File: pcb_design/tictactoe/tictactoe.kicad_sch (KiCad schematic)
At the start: 9 parts

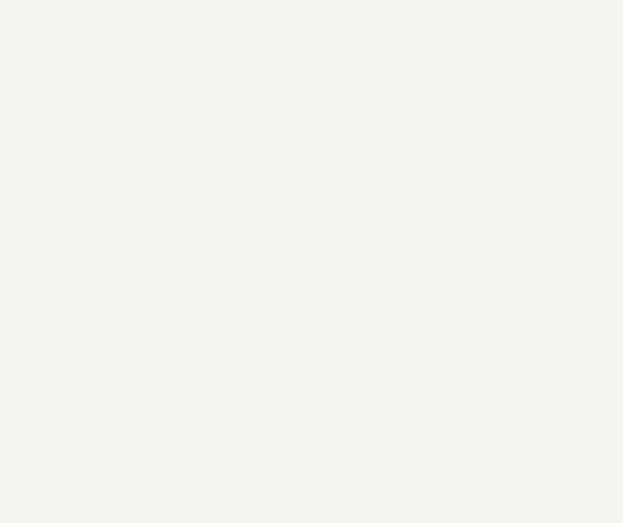
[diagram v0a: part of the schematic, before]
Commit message: NH: Added tactile button to schematic
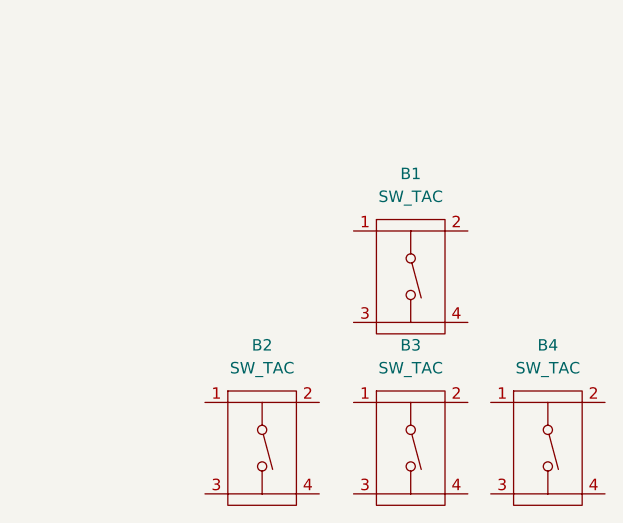
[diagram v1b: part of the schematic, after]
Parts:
- added B1, B2, B3, B4: SW_TAC, symbol TicTacToe:SW_TAC
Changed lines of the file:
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@@
+    (pin "4")
+  )
+  (symbol (lib_id "TicTacToe:SW_TAC") (at 214.63 133.35 0) (unit 1)
+    (in_bom yes) (on_board yes) (fields_autoplaced)
+    (property "Reference" "B2" (id 0) (at 214.63 129.54 0))
+    (property "Value" "SW_TAC" (id 1) (at 214.63 132.08 0))
+    (property "Footprint" "" (id 2) (at 214.63 133.35 0)
+      (effects (font (size 1.27 1.27)) hide)
+    )
+    (property "Datasheet" "" (id 3) (at 214.63 133.35 0)
+      (effects (font (size 1.27 1.27)) hide)
+    )
+    (pin "1")
+    (pin "2")
+    (pin "3")
     (pin "4")
   )
@@
     (pin "4")
   )
+  (symbol (lib_id "TicTacToe:SW_TAC") (at 231.14 133.35 0) (unit 1)
+    (in_bom yes) (on_board yes) (fields_autoplaced)
+    (property "Reference" "B3" (id 0) (at 231.14 129.54 0))
+    (property "Value" "SW_TAC" (id 1) (at 231.14 132.08 0))
+    (property "Footprint" "" (id 2) (at 231.14 133.35 0)
+      (effects (font (size 1.27 1.27)) hide)
+    )
+    (property "Datasheet" "" (id 3) (at 231.14 133.35 0)
+      (effects (font (size 1.27 1.27)) hide)
+    )
+    (pin "1")
+    (pin "2")
+    (pin "3")
+    (pin "4")
+  )
+  (symbol (lib_id "TicTacToe:SW_TAC") (at 246.38 133.35 0) (unit 1)
+    (in_bom yes) (on_board yes) (fields_autoplaced)
+    (property "Reference" "B4" (id 0) (at 246.38 129.54 0))
+    (property "Value" "SW_TAC" (id 1) (at 246.38 132.08 0))
+    (property "Footprint" "" (id 2) (at 246.38 133.35 0)
+      (effects (font (size 1.27 1.27)) hide)
+    )
+    (property "Datasheet" "" (id 3) (at 246.38 133.35 0)
+      (effects (font (size 1.27 1.27)) hide)
+    )
+    (pin "1")
+    (pin "2")
+    (pin "3")
+    (pin "4")
+  )
   (symbol (lib_id "TicTacToe:LED_RKBG") (at 101.6 82.55 0) (unit 1)
     (in_bom yes) (on_board yes) (fields_autoplaced)
@@
     )
     (property "Datasheet" "" (id 3) (at 118.11 99.06 0)
+      (effects (font (size 1.27 1.27)) hide)
+    )
+    (pin "1")
+    (pin "2")
+    (pin "3")
+    (pin "4")
+  )
+  (symbol (lib_id "TicTacToe:SW_TAC") (at 231.14 114.3 0) (unit 1)
+    (in_bom yes) (on_board yes) (fields_autoplaced)
+    (property "Reference" "B1" (id 0) (at 231.14 110.49 0))
+    (property "Value" "SW_TAC" (id 1) (at 231.14 113.03 0))
+    (property "Footprint" "" (id 2) (at 231.14 114.3 0)
+      (effects (font (size 1.27 1.27)) hide)
+    )
+    (property "Datasheet" "" (id 3) (at 231.14 114.3 0)
       (effects (font (size 1.27 1.27)) hide)
     )
@@
   )
   (symbol_instances
+    (path "/aa708fc2-b438-49ea-b120-f9a0d5ee43b8"
+      (reference "B1") (unit 1) (value "SW_TAC") (footprint "")
+    )
+    (path "/3120edca-f3ac-4080-9688-3c8ffb8c69cf"
+      (reference "B2") (unit 1) (value "SW_TAC") (footprint "")
+    )
+    (path "/51d54f5f-2565-40ce-aa69-ef0cd79d62c3"
+      (reference "B3") (unit 1) (value "SW_TAC") (footprint "")
+    )
+    (path "/528e06d5-3a83-4615-8fca-9359e9a773be"
+      (reference "B4") (unit 1) (value "SW_TAC") (footprint "")
+    )
     (path "/15fe2a57-d9d6-4dca-895c-3b64bb8e4d36"
       (reference "D11") (unit 1) (value "LED_RKBG") (footprint "")
